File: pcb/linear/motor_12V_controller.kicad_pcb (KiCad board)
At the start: 2 copper layers, 68 x 48 mm, 37 parts, among them IC1 RP2040-ZERO, J1 01x02, J2 01x02, U1 LM7805_TO220, U2 L293D

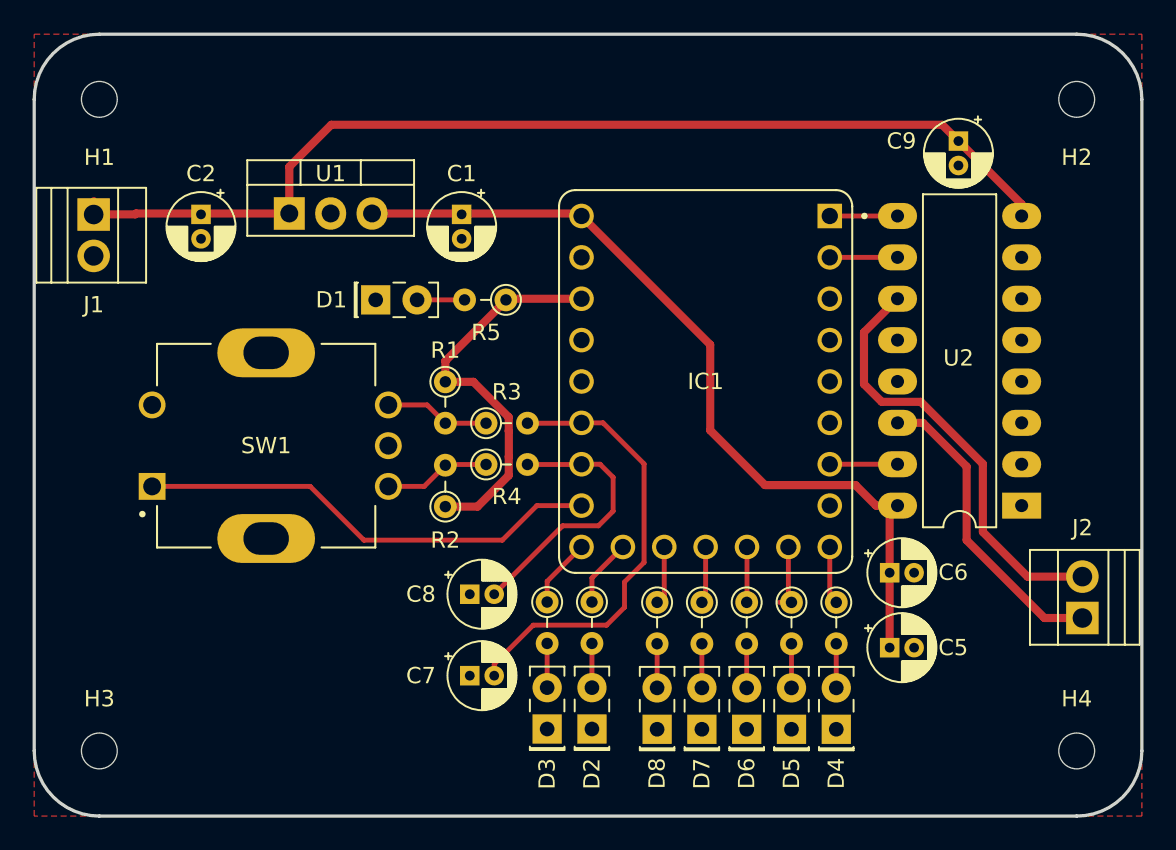
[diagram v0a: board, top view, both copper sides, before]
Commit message: Changed the symbols for THT ceramic capacitors footprint. Swapped the footprints on the PCB design
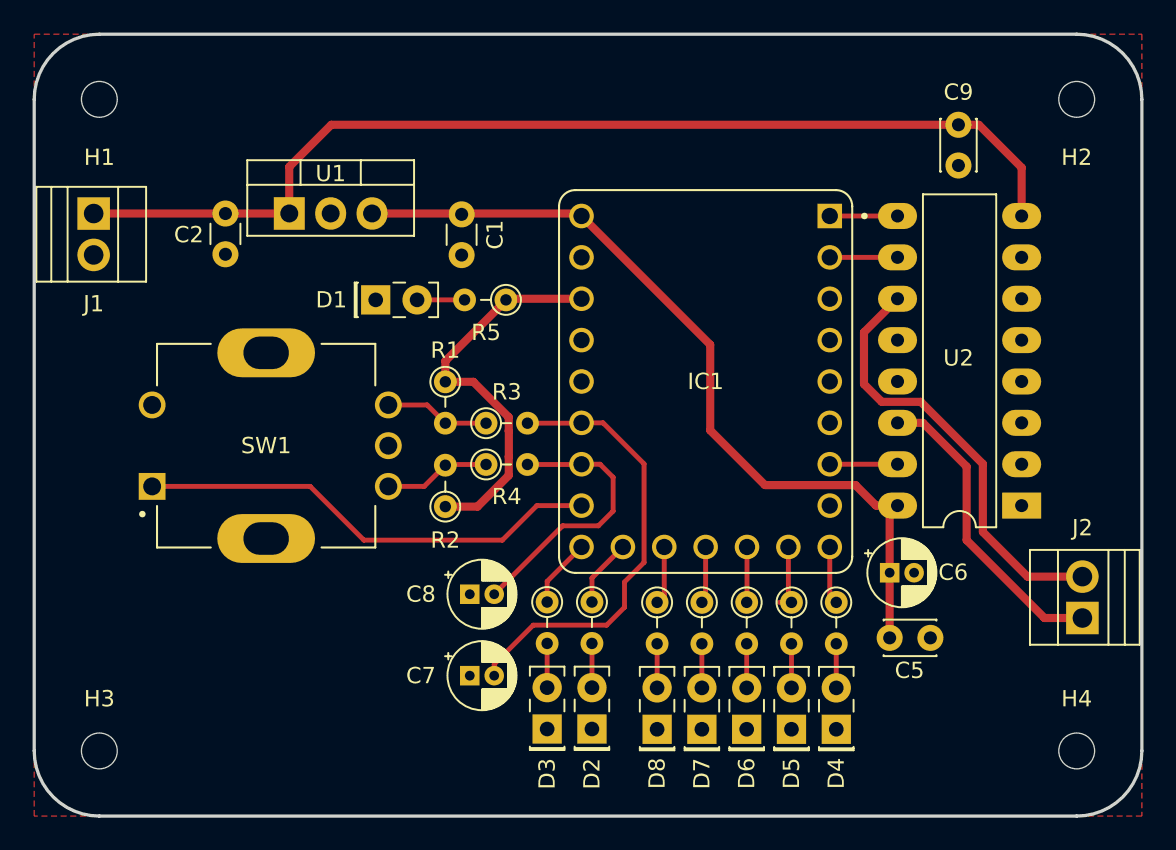
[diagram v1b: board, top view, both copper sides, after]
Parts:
- C1, C2: footprint Capacitor_THT:CP_Radial_D4.0mm_P1.50mm -> Capacitor_THT:C_Disc_D3.0mm_W1.6mm_P2.50mm
- C5, C9: footprint Capacitor_THT:CP_Radial_D4.0mm_P1.50mm -> Capacitor_THT:C_Disc_D3.0mm_W2.0mm_P2.50mm
- moved C2 1.50 mm to (128.0, 80.0)
- moved C9 1.00 mm to (173.0, 74.5)
- moved C5 0.60 mm to (168.8, 106.0)
- moved J1 0.06 mm to (119.9, 80.0)
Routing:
- net +12V: track 63.7 -> 65.0 mm
- net +5V: track 51.7 -> 51.1 mm

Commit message: Added additional RC filtering for the encoder's switch.
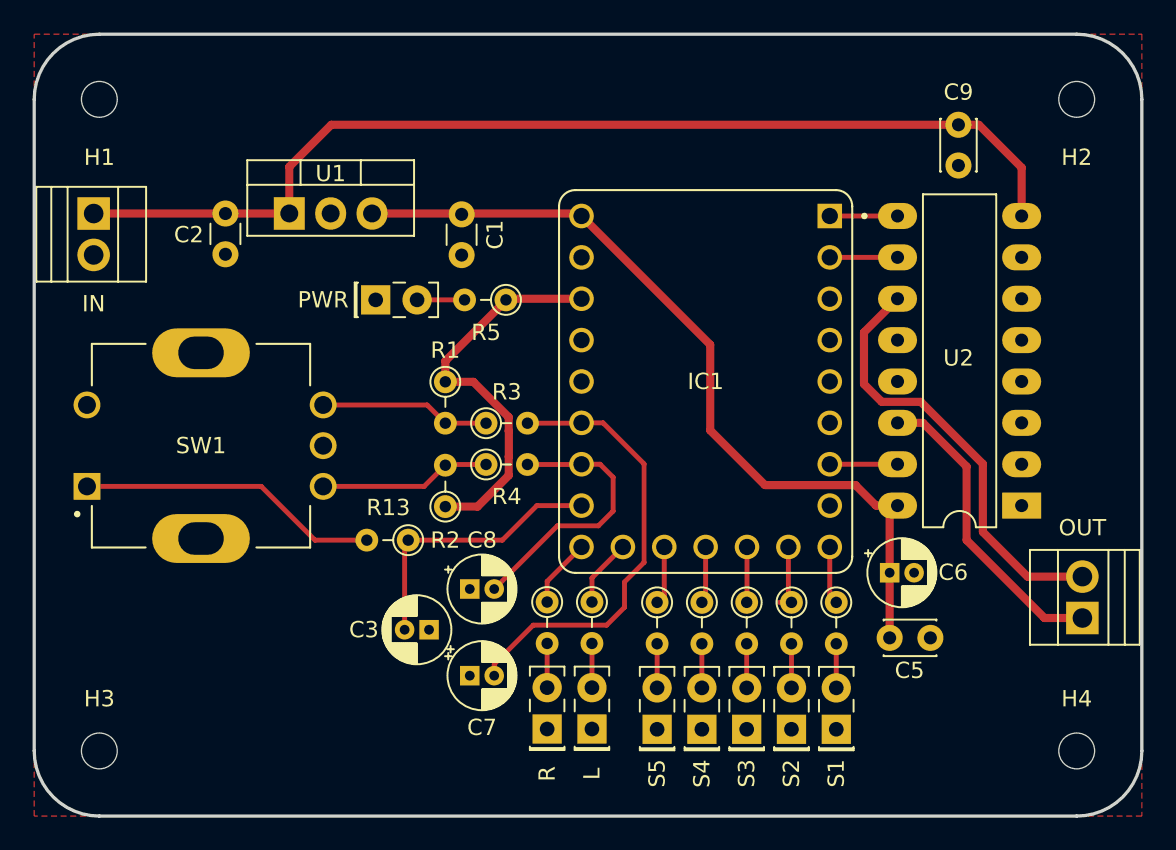
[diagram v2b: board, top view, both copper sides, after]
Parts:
- added C3: 0.1uf, Capacitor_THT:CP_Radial_D4.0mm_P1.50mm, F.Cu at (140.5, 105.5)
- added R13: 10K, Resistor_THT:R_Axial_DIN0204_L3.6mm_D1.6mm_P2.54mm_Vertical, F.Cu at (139.2, 100.0)
- moved SW1 4.00 mm to (126.5, 94.2)
- moved C8 0.32 mm to (143.0, 103.0)
- renumbered J1 to IN, D2 to L, J2 to OUT, D1 to PWR, D3 to R, D4 to S1, D5 to S2, D6 to S3, D7 to S4, D8 to S5
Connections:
- SW1 pad S1: SW -> Net-(R13-Pad2)
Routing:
- net Net-(R13-Pad2): track 0.00 -> 18.5 mm
- net SW: track 28.6 -> 17.1 mm
- net Net-(R1-Pad2): track 6.47 -> 10.5 mm
- net Net-(R2-Pad2): track 6.96 -> 11.0 mm

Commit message: Removed the unecessary RC filter. Purely software debouncing will be used for the switch interface.
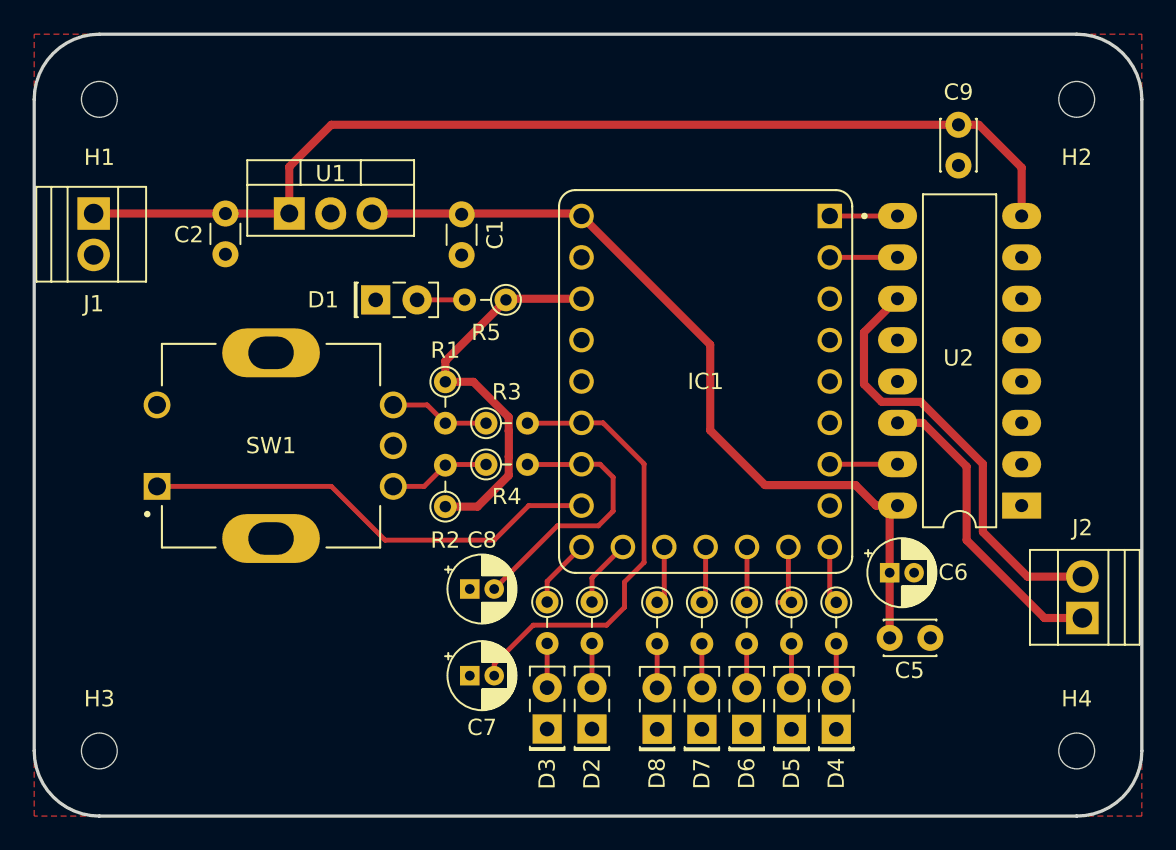
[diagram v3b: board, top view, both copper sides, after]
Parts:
- removed C3: 0.1uf, Capacitor_THT:CP_Radial_D4.0mm_P1.50mm
- removed R13: 10K, Resistor_THT:R_Axial_DIN0204_L3.6mm_D1.6mm_P2.54mm_Vertical
- moved SW1 4.30 mm to (130.8, 94.2)
- renumbered PWR to D1, L to D2, R to D3, S1 to D4, S2 to D5, S3 to D6, S4 to D7, S5 to D8, IN to J1, OUT to J2
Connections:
- SW1 pad S1: Net-(R13-Pad2) -> SW
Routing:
- net Net-(R13-Pad2): track 18.5 -> 0.00 mm
- net SW: track 17.1 -> 28.3 mm
- net Net-(R1-Pad2): track 10.5 -> 6.17 mm
- net Net-(R2-Pad2): track 11.0 -> 6.66 mm
